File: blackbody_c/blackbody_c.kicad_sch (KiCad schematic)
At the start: 0 parts

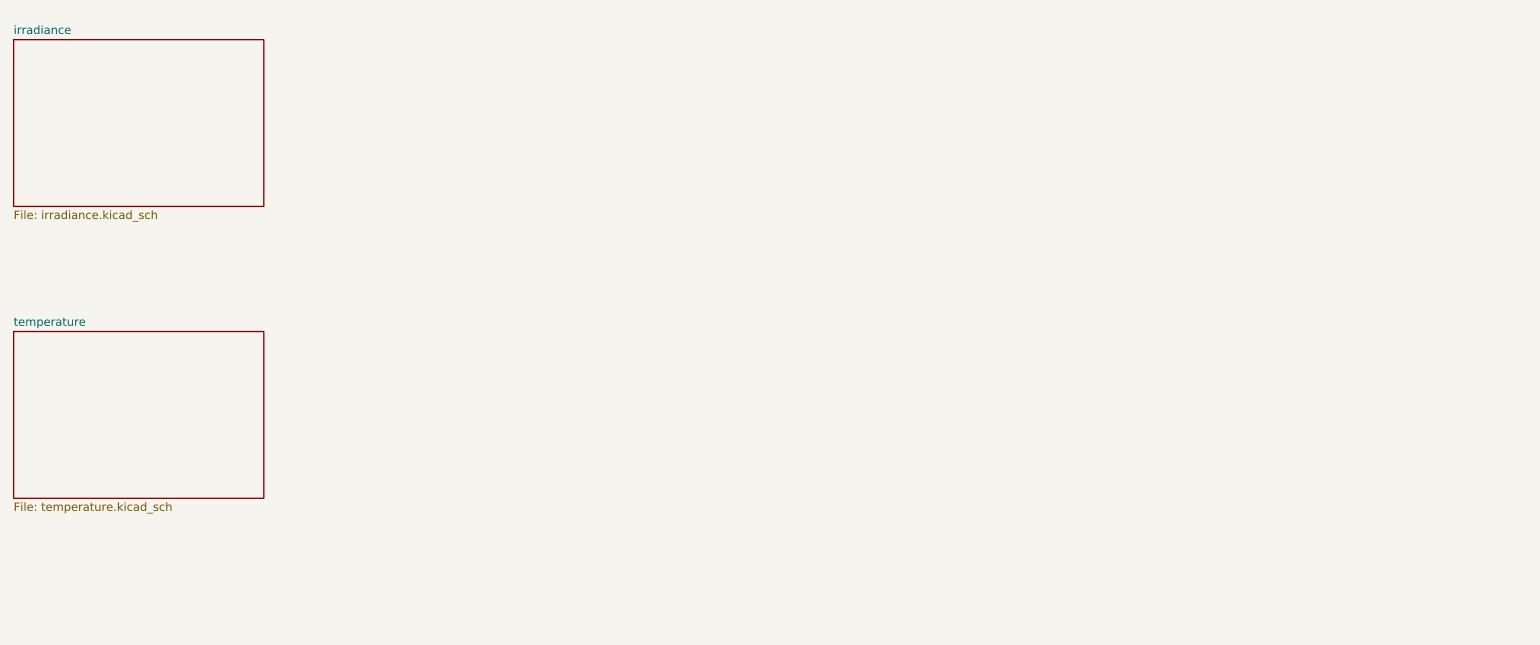
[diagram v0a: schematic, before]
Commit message: added more complexity + thermistor connection
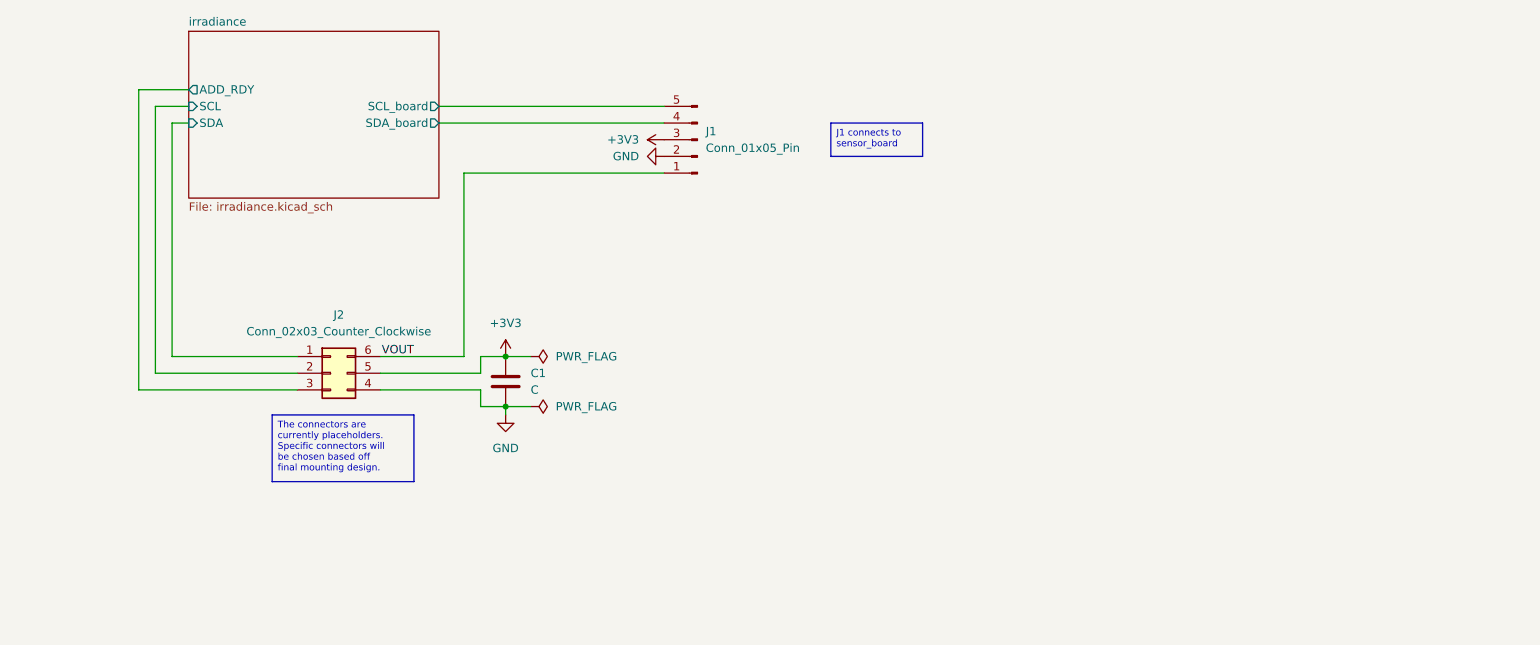
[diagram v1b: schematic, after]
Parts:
- added C1: C, symbol Device:C
- added J1: Conn_01x05_Pin, symbol Connector:Conn_01x05_Pin
- added J2: Conn_02x03_Counter_Clockwise, symbol Connector_Generic:Conn_02x03_Counter_Clockwise
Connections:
- new net +3V3: C1.1, J1.3 (Pin_3), J2.5 (Pin_5)
- new net GND: C1.2, J1.2 (Pin_2), J2.4 (Pin_4)
- new net VOUT: J1.1 (Pin_1), J2.6 (Pin_6)
- new net irradiance/ADD_RDY: J2.3 (Pin_3)
- new net irradiance/SCL: J2.2 (Pin_2)
- new net irradiance/SCL_board: J1.5 (Pin_5)
- new net irradiance/SDA: J2.1 (Pin_1)
- new net irradiance/SDA_board: J1.4 (Pin_4)
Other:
- removed sheet temperature
- sheet irradiance ports: added ADD_RDY, SCL, SCL_board, SDA, SDA_board; removed none

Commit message: Initial version of sensor communication through all three boards
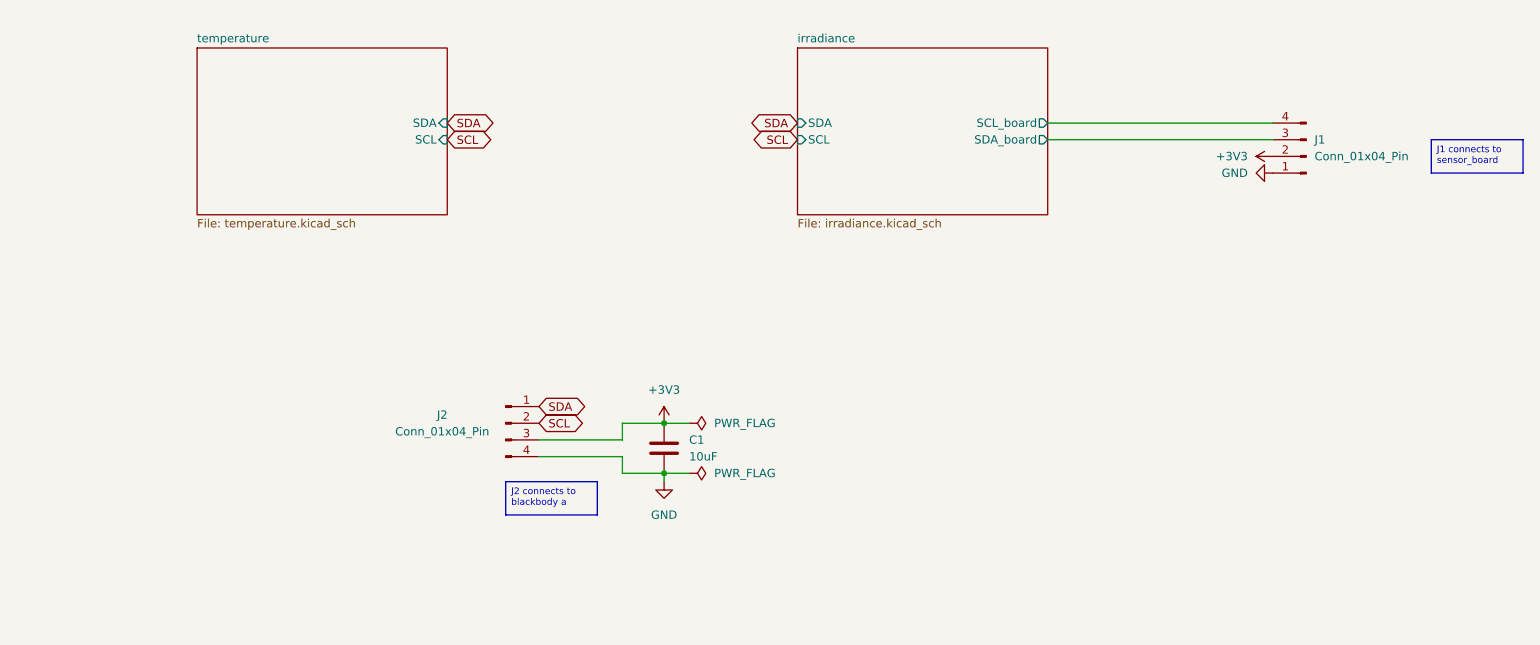
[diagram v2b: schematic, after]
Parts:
- removed J1: Conn_01x05_Pin, symbol Connector:Conn_01x05_Pin
- removed J2: Conn_02x03_Counter_Clockwise, symbol Connector_Generic:Conn_02x03_Counter_Clockwise
- added J1, J2: Conn_01x04_Pin, symbol Connector:Conn_01x04_Pin
- C1: value C -> 10uF
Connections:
- net +3V3: now also J1.2 (Pin_2), J2.3 (Pin_3)
- net GND: now also J1.1 (Pin_1), J2.4 (Pin_4)
- net irradiance/SCL_board: now also J1.4 (Pin_4)
- net irradiance/SDA_board: now also J1.3 (Pin_3)
- new net SCL: J2.2 (Pin_2)
- new net SDA: J2.1 (Pin_1)
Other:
- added sheet temperature (temperature.kicad_sch)
- sheet irradiance ports: added none; removed ADD_RDY
- moved on the sheet: C1

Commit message: Updated minor errors
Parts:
- added J4: Conn_01x04_Pin, symbol Connector:Conn_01x04_Pin
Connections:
- net +3V3: now also J4.2 (Pin_2)
- net GND: now also J4.1 (Pin_1)
- net SCL: now also J4.3 (Pin_3)
- net SDA: now also J4.4 (Pin_4)
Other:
- moved on the sheet: C1, J2

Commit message: Fixed pins, minor changes, removed power isolation
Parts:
- removed C1: 10uF, symbol Device:C
- removed J1, J2, J4: Conn_01x04_Pin, symbol Connector:Conn_01x04_Pin
- added BlackbodyA, BlackbodyA1, BlackbodyC: Conn_01x04, symbol Connector_Generic:Conn_01x04
- added C4: 10uF, symbol Device:C
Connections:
- net +3V3: now also BlackbodyA.3 (Pin_3), BlackbodyA1.3 (Pin_3), BlackbodyC.3 (Pin_3), C4.1
- net GND: now also BlackbodyA.4 (Pin_4), BlackbodyA1.4 (Pin_4), BlackbodyC.4 (Pin_4), C4.2
- net SCL: now also BlackbodyA.2 (Pin_2), BlackbodyC.2 (Pin_2)
- net SDA: now also BlackbodyA.1 (Pin_1), BlackbodyC.1 (Pin_1)
- net irradiance/SCL_board: now also BlackbodyA1.1 (Pin_1)
- net irradiance/SDA_board: now also BlackbodyA1.2 (Pin_2)

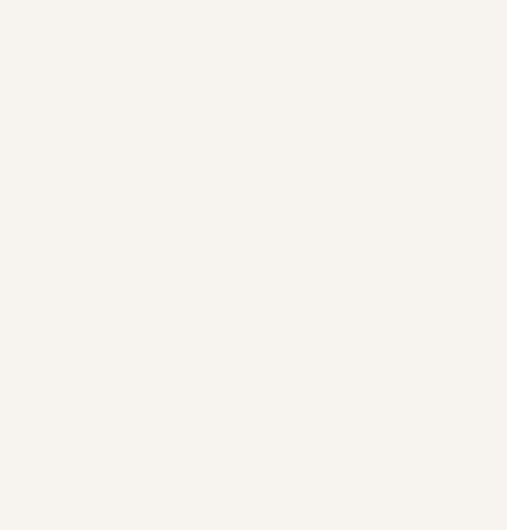
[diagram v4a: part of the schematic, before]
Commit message: add testpoints
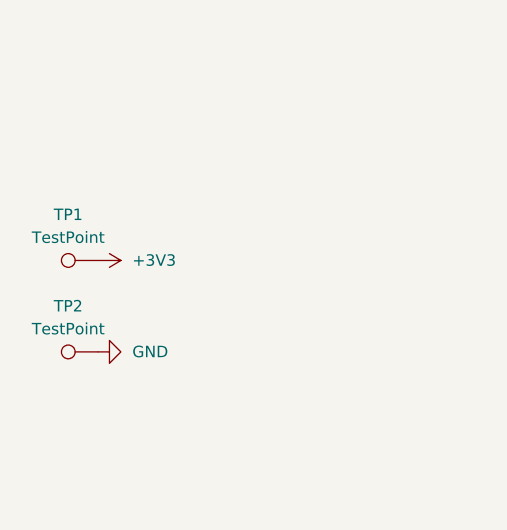
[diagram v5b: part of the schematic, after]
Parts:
- added TP1, TP2: TestPoint, symbol Connector:TestPoint
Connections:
- net +3V3: now also TP1.1
- net GND: now also TP2.1

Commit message: layout iteration 1
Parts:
- BlackbodyA1: renamed from BlackbodyA; footprint (none) -> Blackbodies:MOLEX_1053091104
- BlackbodyC1: renamed from BlackbodyC; footprint (none) -> Blackbodies:MOLEX_1053091104
- C4: footprint (none) -> Capacitor_SMD:C_0805_2012Metric
- SensorBoard1: renamed from BlackbodyA1; footprint (none) -> Blackbodies:CONN_SD-105310-100_04_MOL
- TP1, TP2: footprint (none) -> UTSVT_Special:TestPoint_HEX_3mmID
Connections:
- net irradiance/SCL_board: now also SensorBoard1.2 (Pin_2); no longer SensorBoard1.1 (Pin_1)
- net irradiance/SDA_board: now also SensorBoard1.1 (Pin_1); no longer SensorBoard1.2 (Pin_2)
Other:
- moved on the sheet: BlackbodyA1, BlackbodyC1, C4, SensorBoard1, TP1, TP2

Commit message: layout edits
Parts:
- added H1, H2, H3, H4: MountingHole, MountingHole:MountingHole_3.2mm_M3, symbol Mechanical:MountingHole
- BlackbodyA1, BlackbodyC1: footprint Blackbodies:MOLEX_1053091104 -> Connector_Molex:Molex_Nano-Fit_105313-xx04_1x04_P2.50mm_Horizontal
- SensorBoard1: footprint Blackbodies:CONN_SD-105310-100_04_MOL -> Connector_Molex:Molex_Nano-Fit_105314-xx04_2x02_P2.50mm_Horizontal
- TP1, TP2: footprint UTSVT_Special:TestPoint_HEX_3mmID -> TestPoint:TestPoint_Pad_D1.0mm
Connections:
- net +3V3: now also SensorBoard1.4 (Pin_4); no longer SensorBoard1.3 (Pin_3)
- net GND: now also SensorBoard1.3 (Pin_3); no longer SensorBoard1.4 (Pin_4)
- net SCL: now also BlackbodyA1.1 (Pin_1), BlackbodyC1.1 (Pin_1); no longer BlackbodyA1.2 (Pin_2), BlackbodyC1.2 (Pin_2)
- net SDA: now also BlackbodyA1.2 (Pin_2), BlackbodyC1.2 (Pin_2); no longer BlackbodyA1.1 (Pin_1), BlackbodyC1.1 (Pin_1)
- net irradiance/SCL_board: now also SensorBoard1.1 (Pin_1); no longer SensorBoard1.2 (Pin_2)
- net irradiance/SDA_board: now also SensorBoard1.2 (Pin_2); no longer SensorBoard1.1 (Pin_1)

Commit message: layout updates
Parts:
- added D5: Power, LED_SMD:LED_0805_2012Metric, symbol Device:LED
- added J1: Conn_01x02, Connector_PinHeader_2.54mm:PinHeader_1x02_P2.54mm_Vertical, symbol Connector_Generic:Conn_01x02
- added R22: 2.2k, Resistor_SMD:R_0805_2012Metric, symbol Device:R
- BlackbodyA1, BlackbodyC1: PN (none) -> 105313-1104
- C4: PN (none) -> TMK212BBJ106MGHT
- SensorBoard1: footprint Connector_Molex:Molex_Nano-Fit_105314-xx04_2x02_P2.50mm_Horizontal -> Blackbodies:1054051104; PN (none) -> 105405-2304
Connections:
- net +3V3: now also R22.1
- net GND: now also D5.1 (K)
- net SCL: now also J1.1 (Pin_1)
- net SDA: now also J1.2 (Pin_2)
- new net: D5.2 (A), R22.2
